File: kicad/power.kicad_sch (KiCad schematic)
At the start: 7 parts, among them U1 AP63203WU, U6 TPS54560BDDAR, U7 AP61300Z6

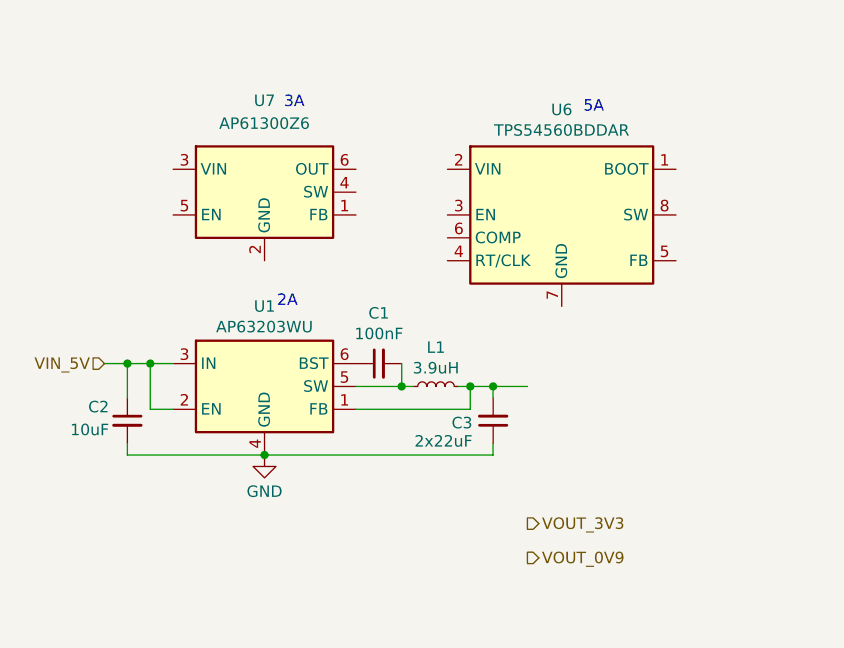
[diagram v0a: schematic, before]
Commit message: Update buck converters
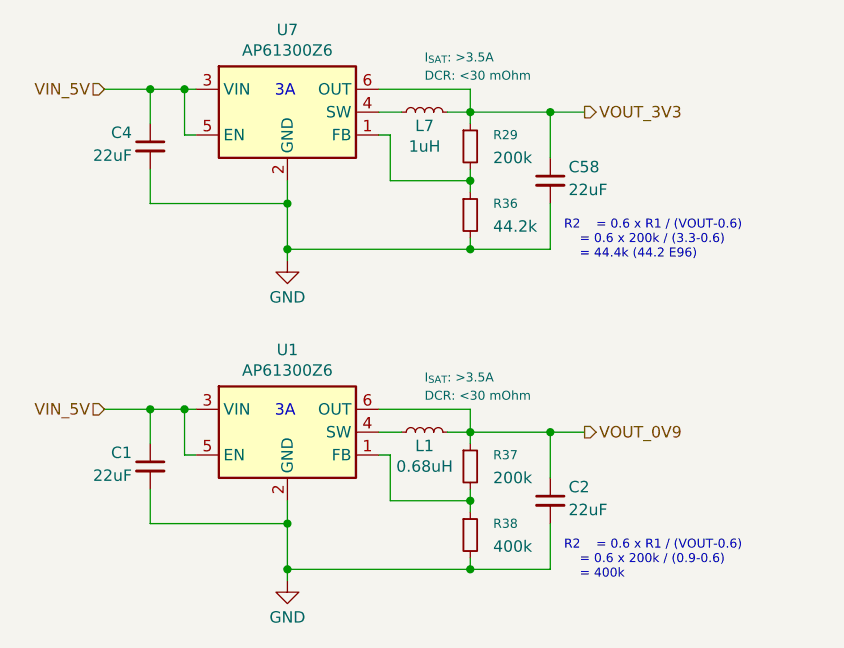
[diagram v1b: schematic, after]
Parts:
- removed C3: 2x22uF, symbol Device:C_Small
- removed U1: AP63203WU, Package_TO_SOT_SMD:TSOT-23-6, symbol Regulator_Switching:AP63203WU
- removed U6: TPS54560BDDAR, Package_SO:Texas_R-PDSO-G8_EP2.95x4.9mm_Mask2.4x3.1mm_ThermalVias, symbol Regulator_Switching:TPS54560BDDA
- added C4, C58: 22uF, symbol Device:C_Small
- added L7: 1uH, symbol Device:L_Small
- added R29, R37: 200k, symbol Device:R_Small
- added R36: 44.2k, symbol Device:R_Small
- added R38: 400k, symbol Device:R_Small
- added U1: AP61300Z6, Package_TO_SOT_SMD:SOT-563, symbol Regulator_Switching:AP61300Z6
- C1: value 100nF -> 22uF
- C2: value 10uF -> 22uF
- L1: value 3.9uH -> 0.68uH; DCR (none) -> <30 mOhm; I_{SAT} (none) -> >3.5A
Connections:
- net GND: now also C1.2, U7.2 (GND), C4.2, C58.2, R36.2, R38.2, U1.2 (GND)
- net VIN_5V: now also C1.1, U7.3 (VIN), U7.5 (EN), C4.1, U1.3 (VIN), U1.5 (EN); no longer C2.1
- net VOUT_0V9: now also C2.1, L1.2, R37.1, U1.6 (OUT)
- net VOUT_3V3: now also U7.6 (OUT), C58.1, L7.2, R29.1
- net at L1.1: now also U1.4 (SW); no longer C1.2
- net at U7.1 (FB): now also R29.2, R36.1
- net at U7.4 (SW): now also L7.1
- new net: R37.2, R38.1, U1.1 (FB)
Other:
- note added: "R2 = 0.6 x R1 / (VOUT-0.6) = 0.6 x 200k / (0.9-0.6) = 400k"
- note added: "R2 = 0.6 x R1 / (VOUT-0.6) = 0.6 x 200k / (3.3-0.6) = 44.4k (44.2 E96)"
- note removed: "2A"
- note removed: "5A"
- moved on the sheet: U7

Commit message: Add power supply and ll shifter
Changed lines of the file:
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@@
 		(dnp no)
 		(property "Reference" "L1"
-			(at 73.6537 63.754 90)
+			(at 72.136 55.88 90)
 			(effects
 				(font
@@
 		)
 		(property "Value" "0.68uH"
-			(at 73.66 66.04 90)
+			(at 72.1423 58.166 90)
 			(effects
 				(font
@@
 		)
 		(property "I_{SAT}" ">3.5A"
-			(at 73.66 56.134 90)
+			(at 76.454 56.134 90)
 			(show_name yes)
 			(effects
@@
 		)
 		(property "DCR" "<30 mOhm"
-			(at 73.66 58.166 90)
+			(at 76.454 58.166 90)
 			(show_name yes)
 			(effects
@@
 		(dnp no)
 		(property "Reference" "L7"
-			(at 73.6537 28.194 90)
+			(at 72.136 20.32 90)
 			(effects
 				(font
@@
 		)
 		(property "Value" "1uH"
-			(at 73.66 30.48 90)
+			(at 72.1423 22.606 90)
 			(effects
 				(font
@@
 		)
 		(property "I_{SAT}" ">3.5A"
-			(at 73.66 20.574 90)
+			(at 76.454 20.574 90)
 			(show_name yes)
 			(effects
@@
 		)
 		(property "DCR" "<30 mOhm"
-			(at 73.66 22.606 90)
+			(at 76.454 22.606 90)
 			(show_name yes)
 			(effects
